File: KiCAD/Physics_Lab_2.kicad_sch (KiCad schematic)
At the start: 8 parts, among them J1 USB_C, U1 MCP73871

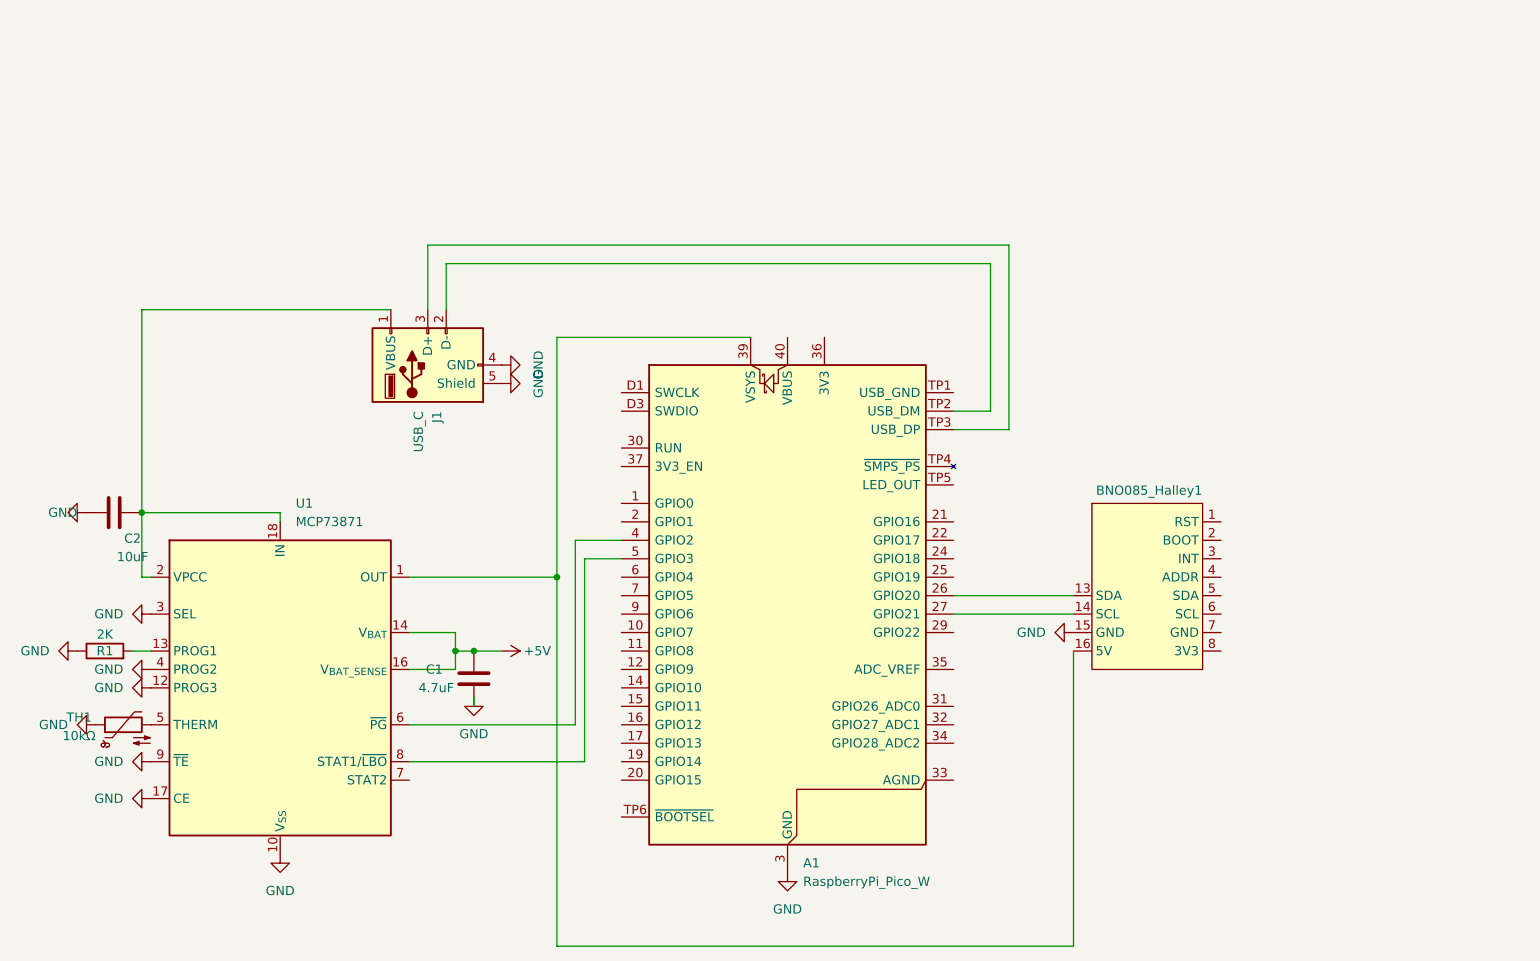
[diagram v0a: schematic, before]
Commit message: Fix merge conflict by pause
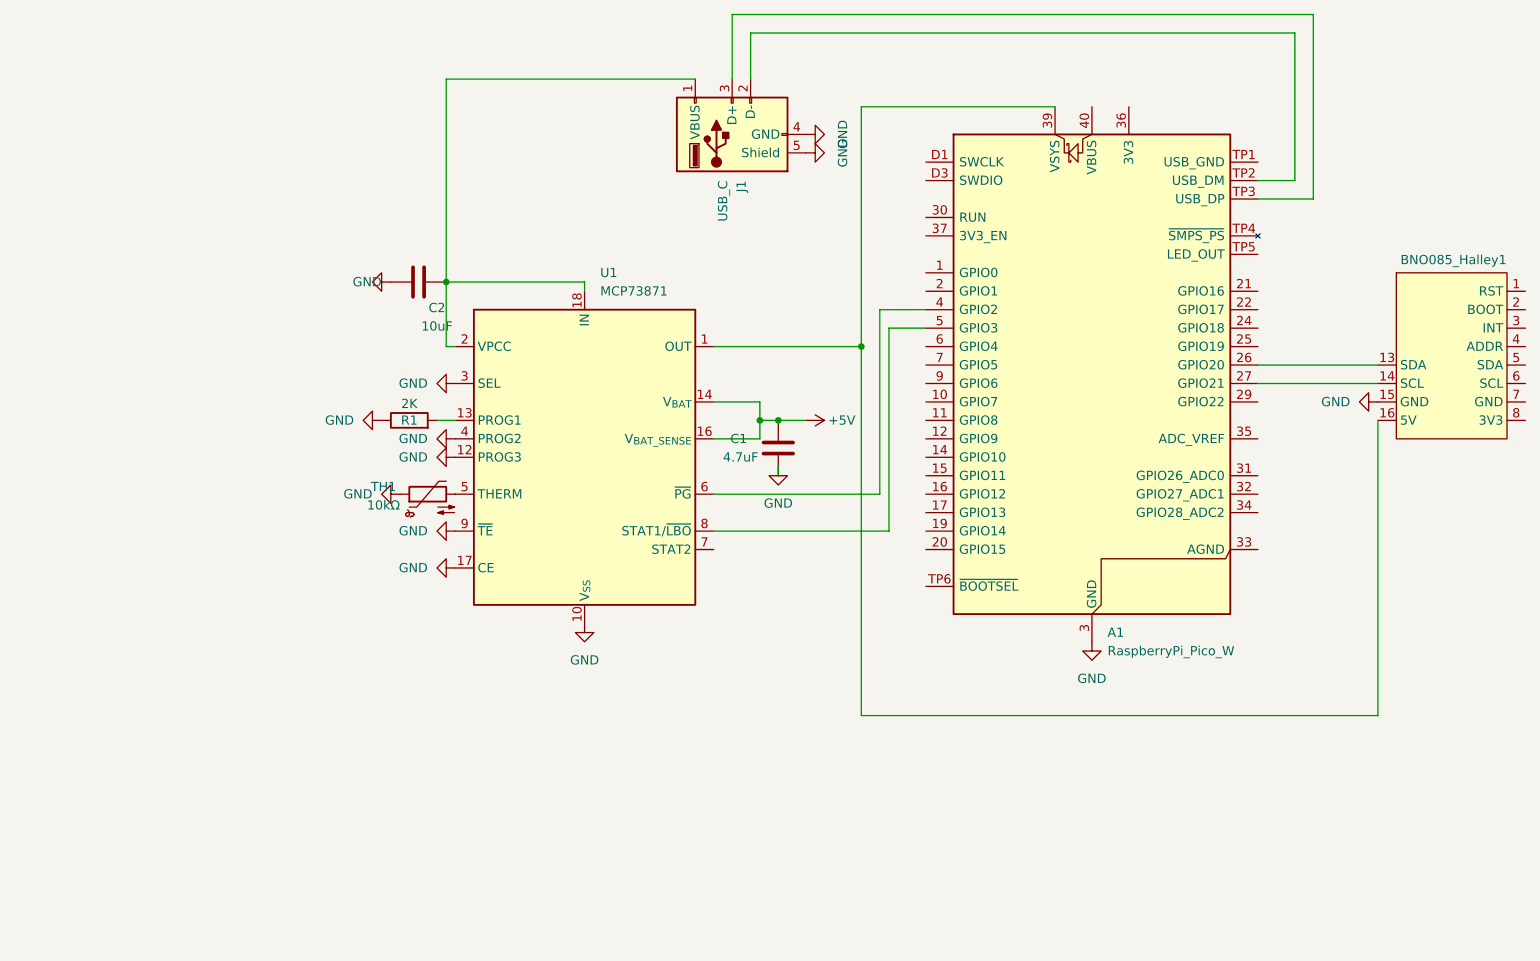
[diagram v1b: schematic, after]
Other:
- moved on the sheet: A1, BNO085_Halley1, C1, C2, J1, R1, TH1, U1

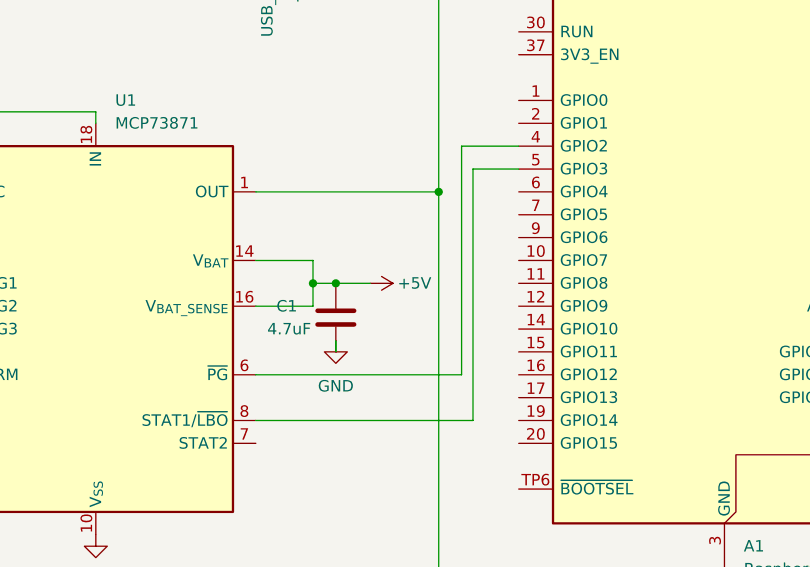
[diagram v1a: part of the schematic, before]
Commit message: Fix wiring to battery and grounding
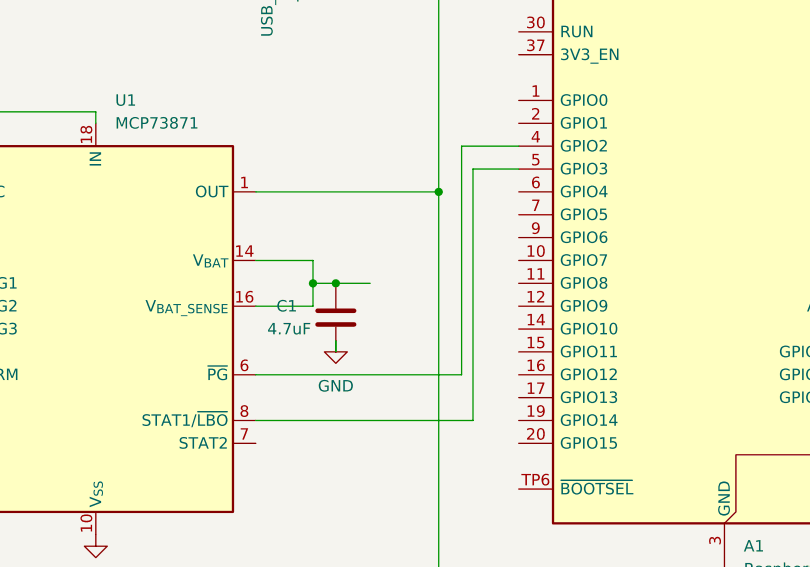
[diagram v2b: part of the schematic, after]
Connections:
- net +5V: no longer names the net of C1.1, U1.14 (V_{BAT}), U1.15 (V_{BAT}), U1.16 (V_{BAT_SENSE})
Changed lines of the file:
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@@
-	)
-	(symbol
-		(lib_id "power:+5V")
-		(at 127 104.14 270)
-		(unit 1)
-		(exclude_from_sim no)
-		(in_bom yes)
-		(on_board yes)
-		(dnp no)
-		(property "Reference" "#PWR09"
-			(at 123.19 104.14 0)
-			(effects
-				(font
-					(size 1.27 1.27)
-				)
-				(hide yes)
-			)
-		)
-		(property "Value" "+5V"
-			(at 130.048 104.14 90)
-			(effects
-				(font
-					(size 1.27 1.27)
-				)
-				(justify left)
-			)
-		)
-		(property "Footprint" ""
-			(at 127 104.14 0)
-			(effects
-				(font
-					(size 1.27 1.27)
-				)
-				(hide yes)
-			)
-		)
-		(property "Datasheet" ""
-			(at 127 104.14 0)
-			(effects
-				(font
-					(size 1.27 1.27)
-				)
-				(hide yes)
-			)
-		)
-		(property "Description" "Power symbol creates a global label with name \"+5V\""
-			(at 127 104.14 0)
-			(effects
-				(font
-					(size 1.27 1.27)
-				)
-				(hide yes)
-			)
-		)
-		(pin "1"
-		)
-		(instances
-			(project ""
-				(path "/2bf0a60c-6e8f-4203-b806-d9c74a7dd08d"
-					(reference "#PWR09")
-					(unit 1)
-				)
-			)
-		)
 	)
 	(symbol
